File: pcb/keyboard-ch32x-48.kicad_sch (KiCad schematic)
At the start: 116 parts, among them J1 USB_C_Receptacle_USB2.0, J2 Conn_01x02, J3 Conn_01x04, SW1 SW_SPST, SW2 SW_SPST, U1 CH32X033F8P6

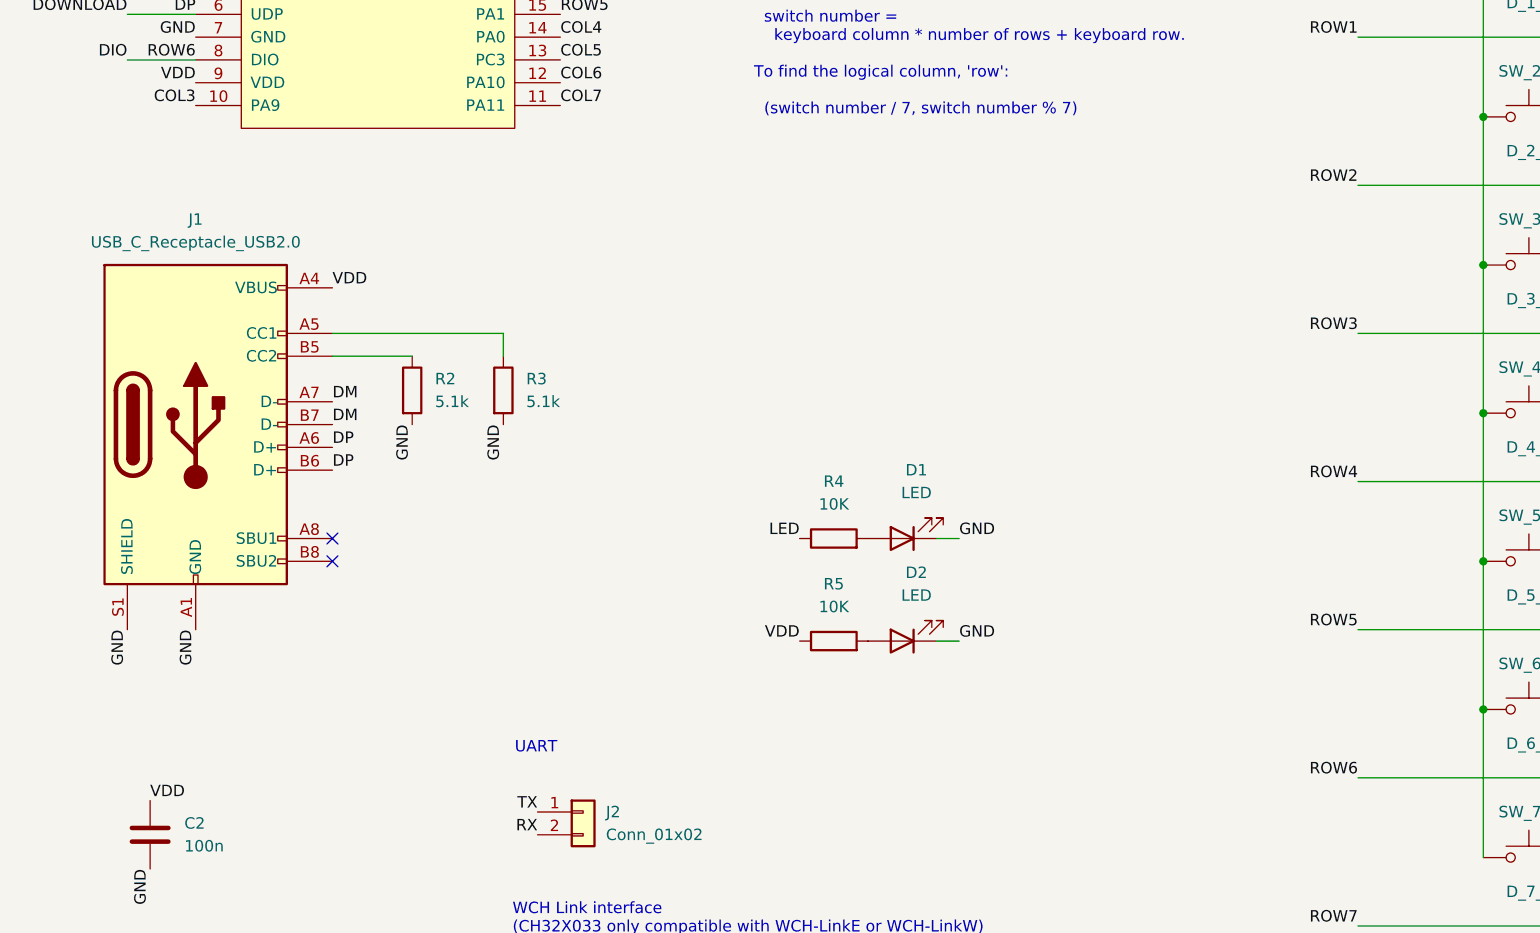
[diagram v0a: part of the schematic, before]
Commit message: pcb: ch32x-48: add notes to schematic
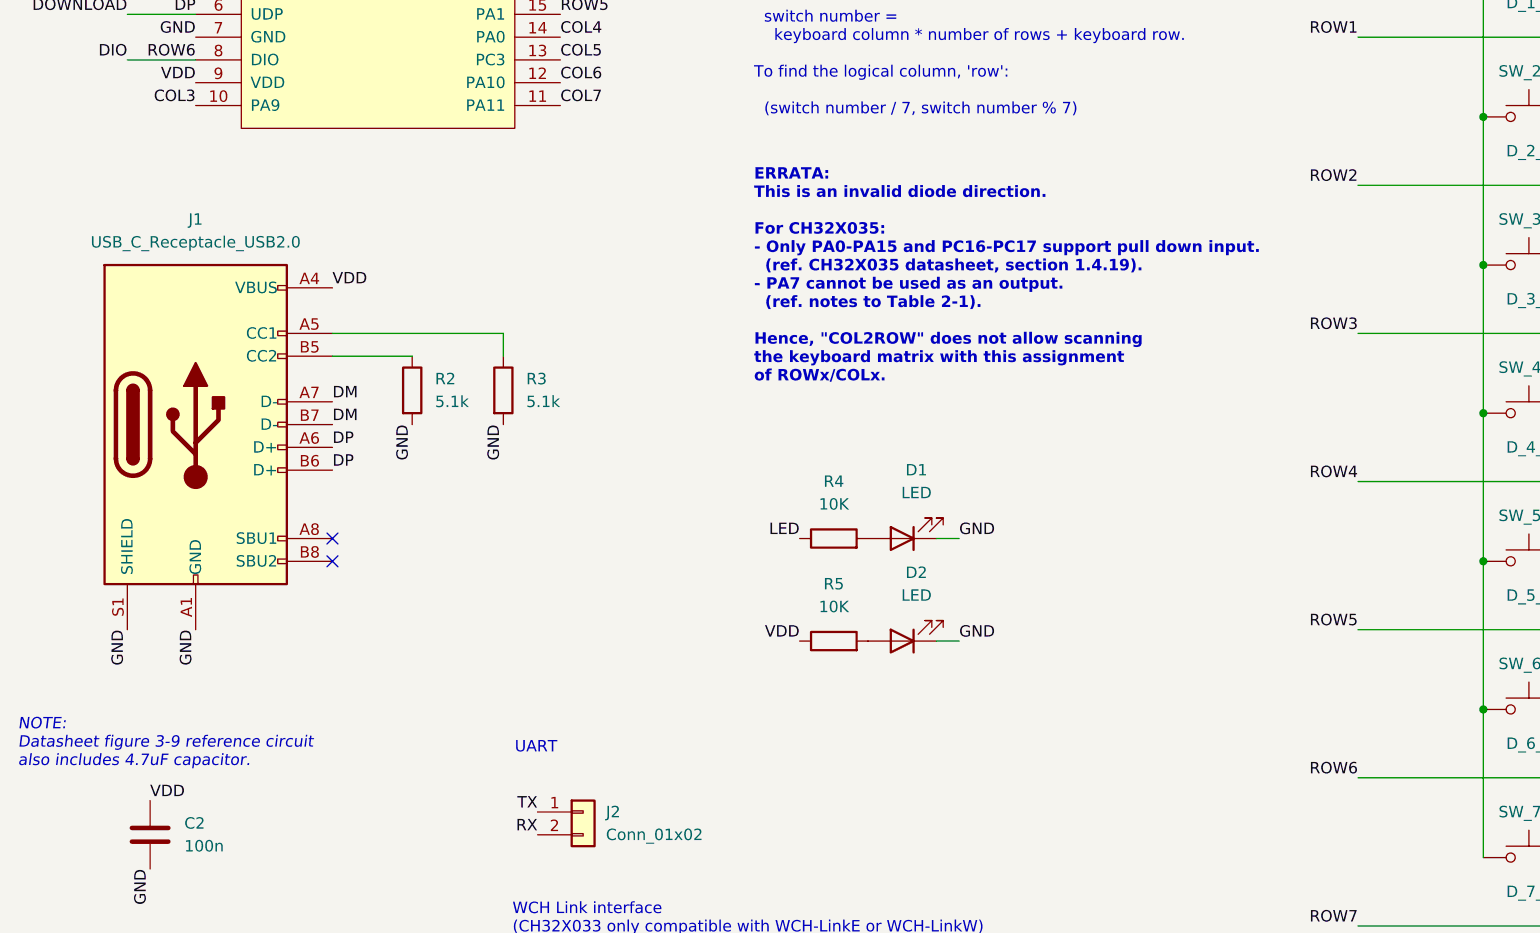
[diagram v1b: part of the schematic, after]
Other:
- note added: "ERRATA: This is an invalid diode direction. For CH32X035: - Only PA0-PA15 and PC16-PC17 support pull down input. (ref. CH32X035 datasheet, section 1.4.19). - PA7 cannot be used as an output. (ref. notes to Table 2-1). Hence, "COL2ROW" does not allow scanning the keyboard matrix with this assignment of ROWx/COLx."
- note added: "NOTE: Datasheet figure 3-9 reference circuit also includes 4.7uF capacitor."
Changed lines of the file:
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@@
+		)
+	)
+	(text "ERRATA:\nThis is an invalid diode direction.\n\nFor CH32X035:\n- Only PA0-PA15 and PC16-PC17 support pull down input.\n  (ref. CH32X035 datasheet, section 1.4.19).\n- PA7 cannot be used as an output.\n  (ref. notes to Table 2-1).\n\nHence, \"COL2ROW\" does not allow scanning\nthe keyboard matrix with this assignment\nof ROWx/COLx."
+		(exclude_from_sim no)
+		(at 96.52 66.04 0)
+		(effects
+			(font
+				(size 1.27 1.27)
+				(thickness 0.254)
+				(bold yes)
+				(color 255 0 0 1)
+			)
+			(justify left)
 		)
 	)
@@
 		)
 	)
+	(text "NOTE:\nDatasheet figure 3-9 reference circuit\nalso includes 4.7uF capacitor."
+		(exclude_from_sim no)
+		(at 14.478 118.11 0)
+		(effects
+			(font
+				(size 1.27 1.27)
+				(italic yes)
+				(color 0 194 0 1)
+			)
+			(justify left)
+		)
+	)

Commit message: pcb: ch32x-48: rev2025.2
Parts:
- added C3: 4.7uF, Capacitor_SMD:C_0805_2012Metric, symbol Device:C
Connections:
- net DCK: now also D_2_1.2 (A), D_2_2.2 (A), D_2_3.2 (A), D_2_4.2 (A), D_2_5.2 (A), D_2_6.2 (A), D_2_7.2 (A); no longer D_2_1.1 (K), D_2_2.1 (K), D_2_3.1 (K), D_2_4.1 (K), D_2_5.1 (K), D_2_6.1 (K), D_2_7.1 (K)
- net DIO: now also D_6_1.2 (A), D_6_2.2 (A), D_6_3.2 (A), D_6_4.2 (A), D_6_5.2 (A), D_6_6.2 (A), D_6_7.2 (A); no longer D_6_1.1 (K), D_6_2.1 (K), D_6_3.1 (K), D_6_4.1 (K), D_6_5.1 (K), D_6_6.1 (K), D_6_7.1 (K)
- net GND: now also C3.2
- net ROW1: now also D_1_1.2 (A), D_1_2.2 (A), D_1_3.2 (A), D_1_4.2 (A), D_1_5.2 (A), D_1_6.2 (A), D_1_7.2 (A); no longer D_1_1.1 (K), D_1_2.1 (K), D_1_3.1 (K), D_1_4.1 (K), D_1_5.1 (K), D_1_6.1 (K), D_1_7.1 (K)
- net ROW3: now also D_3_1.2 (A), D_3_2.2 (A), D_3_3.2 (A), D_3_4.2 (A), D_3_5.2 (A), D_3_6.2 (A), D_3_7.2 (A); no longer D_3_1.1 (K), D_3_2.1 (K), D_3_3.1 (K), D_3_4.1 (K), D_3_5.1 (K), D_3_6.1 (K), D_3_7.1 (K)
- net ROW4: now also D_4_1.2 (A), D_4_2.2 (A), D_4_3.2 (A), D_4_4.2 (A), D_4_5.2 (A), D_4_6.2 (A), D_4_7.2 (A); no longer D_4_1.1 (K), D_4_2.1 (K), D_4_3.1 (K), D_4_4.1 (K), D_4_5.1 (K), D_4_6.1 (K), D_4_7.1 (K)
- net ROW5: now also D_5_1.2 (A), D_5_2.2 (A), D_5_3.2 (A), D_5_4.2 (A), D_5_5.2 (A), D_5_6.2 (A), D_5_7.2 (A); no longer D_5_1.1 (K), D_5_2.1 (K), D_5_3.1 (K), D_5_4.1 (K), D_5_5.1 (K), D_5_6.1 (K), D_5_7.1 (K)
- net ROW7: now also D_7_1.2 (A), D_7_2.2 (A), D_7_3.2 (A), D_7_4.2 (A), D_7_5.2 (A), D_7_6.2 (A); no longer D_7_1.1 (K), D_7_2.1 (K), D_7_3.1 (K), D_7_4.1 (K), D_7_5.1 (K), D_7_6.1 (K)
- net VDD: now also C3.1
- net at SW_4_1.2: now also D_4_1.1 (K); no longer D_4_1.2 (A)
- net at SW_6_6.2: now also D_6_6.1 (K); no longer D_6_6.2 (A)
- net at SW_3_2.2: now also D_3_2.1 (K); no longer D_3_2.2 (A)
- net at SW_6_2.2: now also D_6_2.1 (K); no longer D_6_2.2 (A)
- net at SW_7_4.2: now also D_7_4.1 (K); no longer D_7_4.2 (A)
- net at SW_6_3.2: now also D_6_3.1 (K); no longer D_6_3.2 (A)
- net at SW_4_5.2: now also D_4_5.1 (K); no longer D_4_5.2 (A)
- net at SW_1_5.2: now also D_1_5.1 (K); no longer D_1_5.2 (A)
- net at SW_4_3.2: now also D_4_3.1 (K); no longer D_4_3.2 (A)
- net at SW_4_4.2: now also D_4_4.1 (K); no longer D_4_4.2 (A)
- net at SW_1_2.2: now also D_1_2.1 (K); no longer D_1_2.2 (A)
- net at SW_1_4.2: now also D_1_4.1 (K); no longer D_1_4.2 (A)
- net at SW_7_1.2: now also D_7_1.1 (K); no longer D_7_1.2 (A)
- net at SW_3_6.2: now also D_3_6.1 (K); no longer D_3_6.2 (A)
- net at SW_7_5.2: now also D_7_5.1 (K); no longer D_7_5.2 (A)
- net at SW_7_3.2: now also D_7_3.1 (K); no longer D_7_3.2 (A)
- net at SW_1_6.2: now also D_1_6.1 (K); no longer D_1_6.2 (A)
- net at SW_7_6.2: now also D_7_6.1 (K); no longer D_7_6.2 (A)
- net at SW_5_4.2: now also D_5_4.1 (K); no longer D_5_4.2 (A)
- net at SW_6_7.2: now also D_6_7.1 (K); no longer D_6_7.2 (A)
- net at SW_3_5.2: now also D_3_5.1 (K); no longer D_3_5.2 (A)
- net at SW_5_1.2: now also D_5_1.1 (K); no longer D_5_1.2 (A)
- net at SW_3_7.2: now also D_3_7.1 (K); no longer D_3_7.2 (A)
- net at SW_2_1.2: now also D_2_1.1 (K); no longer D_2_1.2 (A)
- net at SW_6_5.2: now also D_6_5.1 (K); no longer D_6_5.2 (A)
- net at SW_5_2.2: now also D_5_2.1 (K); no longer D_5_2.2 (A)
- net at SW_2_2.2: now also D_2_2.1 (K); no longer D_2_2.2 (A)
- net at SW_1_3.2: now also D_1_3.1 (K); no longer D_1_3.2 (A)
- net at SW_4_7.2: now also D_4_7.1 (K); no longer D_4_7.2 (A)
- net at SW_4_2.2: now also D_4_2.1 (K); no longer D_4_2.2 (A)
- net at SW_2_3.2: now also D_2_3.1 (K); no longer D_2_3.2 (A)
- net at SW_7_2.2: now also D_7_2.1 (K); no longer D_7_2.2 (A)
- net at SW_2_4.2: now also D_2_4.1 (K); no longer D_2_4.2 (A)
- net at SW_4_6.2: now also D_4_6.1 (K); no longer D_4_6.2 (A)
- net at SW_5_3.2: now also D_5_3.1 (K); no longer D_5_3.2 (A)
- net at SW_5_5.2: now also D_5_5.1 (K); no longer D_5_5.2 (A)
- net at SW_5_7.2: now also D_5_7.1 (K); no longer D_5_7.2 (A)
- net at SW_2_5.2: now also D_2_5.1 (K); no longer D_2_5.2 (A)
- net at SW_2_6.2: now also D_2_6.1 (K); no longer D_2_6.2 (A)
- net at SW_2_7.2: now also D_2_7.1 (K); no longer D_2_7.2 (A)
- net at SW_3_3.2: now also D_3_3.1 (K); no longer D_3_3.2 (A)
- net at SW_6_4.2: now also D_6_4.1 (K); no longer D_6_4.2 (A)
- net at SW_1_7.2: now also D_1_7.1 (K); no longer D_1_7.2 (A)
- net at SW_5_6.2: now also D_5_6.1 (K); no longer D_5_6.2 (A)
- net at SW_6_1.2: now also D_6_1.1 (K); no longer D_6_1.2 (A)
- net at SW_3_1.2: now also D_3_1.1 (K); no longer D_3_1.2 (A)
- net at SW_3_4.2: now also D_3_4.1 (K); no longer D_3_4.2 (A)
- net at SW_1_1.2: now also D_1_1.1 (K); no longer D_1_1.2 (A)
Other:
- note added: "Decoupling capacitors"
- note added: "Download switch. Short while plugging in USB to enter ISP flashing mode. e.g. with wchisp."
- note added: "Hardware, Mounting Holes For M2 screws. Same mounting holes as JJ40."
- note added: "IMPORTANT: Take care with diode direction!"
- note added: "Reset Switch ref. Figure 3-3 Typical circuit of CH32X datasheet."
- note added: "Take care the diode direction agrees with matrix scanning requirements for writing to the pin / pulling down."
- note added: "UART For simple printf debugging with UART2. ("ROW4"/SW_4_x switches can't be used while using UART2)."
- note added: "USB Connector"
- note added: "WCH Link interface (CH32X033 only compatible with WCH-LinkE or WCH-LinkW) Using DIO/DCK prevents use of ROW2/ROW6."
- note removed: "ERRATA: This is an invalid diode direction. For CH32X035: - Only PA0-PA15 and PC16-PC17 support pull down input. (ref. CH32X035 datasheet, section 1.4.19). - PA7 cannot be used as an output. (ref. notes to Table 2-1). Hence, "COL2ROW" does not allow scanning the keyboard matrix with this assignment of ROWx/COLx."
- note removed: "NOTE: Datasheet figure 3-9 reference circuit also includes 4.7uF capacitor."
- note removed: "UART"
- note removed: "WCH Link interface (CH32X033 only compatible with WCH-LinkE or WCH-LinkW)"
- moved on the sheet: C1, C2, D1, D2, D_1_1, D_1_2, D_1_3, D_1_4, D_1_5, D_1_6, D_1_7, D_2_1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

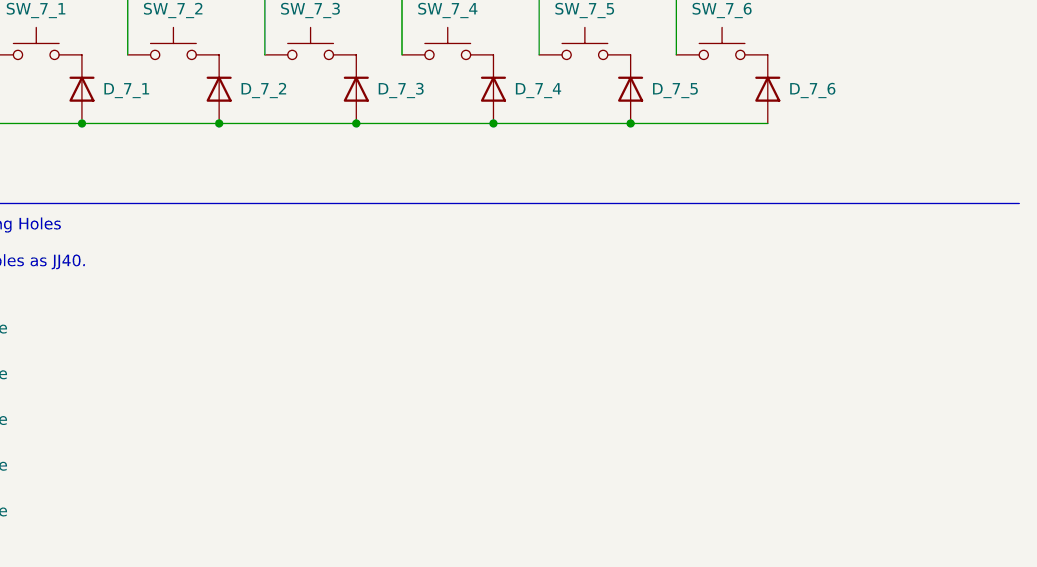
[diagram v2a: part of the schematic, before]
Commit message: pcb: ch32x-48 rev2025.3
rev2025.3:
- increase trace width to 0.25,
  - fix DRC.
- add 10K pullup for Row6 (DIO),
   per testing of the rev2025.1 board.

rev2025.2:
- fixed the diodes to be col2row,
  as the assignments of rows
  (and CH32X limitations on pins)
  required this.
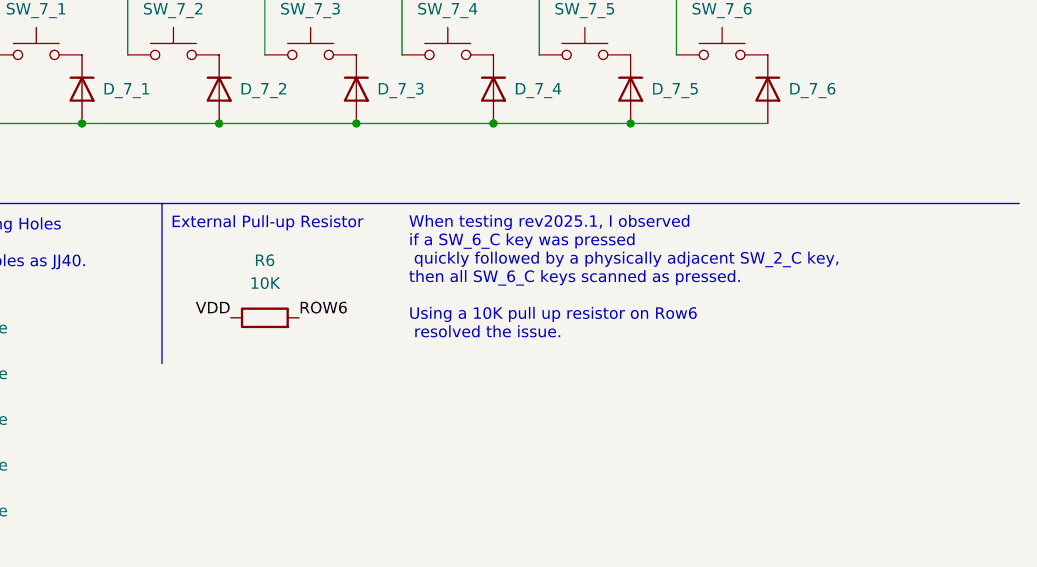
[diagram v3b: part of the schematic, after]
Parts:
- added R6: 10K, Resistor_SMD:R_0805_2012Metric, symbol Device:R
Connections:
- net DIO: now also R6.2
- net VDD: now also R6.1
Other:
- note added: "External Pull-up Resistor"
- note added: "When testing rev2025.1, I observed if a SW_6_C key was pressed quickly followed by a physically adjacent SW_2_C key, then all SW_6_C keys scanned as pressed. Using a 10K pull up resistor on Row6 resolved the issue."
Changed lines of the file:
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@@
 	(title_block
 		(title "CH32X-48")
-		(date "2025-01-10")
-		(rev "rev2025.2")
+		(date "2025-01-16")
+		(rev "rev2025.3")
 		(company "Richard Goulter (rgoulter)")
 		(comment 1 "48-key on 7x7 digital matrix.")
@@
 		)
 	)
+	(polyline
+		(pts
+			(xy 189.23 147.32) (xy 189.23 165.1)
+		)
+		(stroke
+			(width 0)
+			(type default)
+		)
+	)
 	(wire
 		(pts
@@
 		)
 	)
+	(text "External Pull-up Resistor"
+		(exclude_from_sim no)
+		(at 190.246 149.606 0)
+		(effects
+			(font
+				(size 1.27 1.27)
+			)
+			(justify left)
+		)
+	)
 	(text "Reset Switch\nref. Figure 3-3 Typical circuit\nof CH32X datasheet."
 		(exclude_from_sim no)
@@
 		)
 	)
+	(text "When testing rev2025.1, I observed\nif a SW_6_C key was pressed\n quickly followed by a physically adjacent SW_2_C key,\nthen all SW_6_C keys scanned as pressed.\n\nUsing a 10K pull up resistor on Row6\n resolved the issue."
+		(exclude_from_sim no)
+		(at 216.662 155.702 0)
+		(effects
+			(font
+				(size 1.27 1.27)
+			)
+			(justify left)
+		)
+	)
 	(text "Hardware, Mounting Holes\nFor M2 screws.\nSame mounting holes as JJ40."
 		(exclude_from_sim no)
@@
 		)
 	)
+	(label "ROW6"
+		(at 204.47 160.02 0)
+		(fields_autoplaced yes)
+		(effects
+			(font
+				(size 1.27 1.27)
+			)
+			(justify left bottom)
+		)
+	)
 	(label "COL2"
 		(at 34.29 24.13 180)
@@
 		)
 	)
+	(label "VDD"
+		(at 196.85 160.02 180)
+		(fields_autoplaced yes)
+		(effects
+			(font
+				(size 1.27 1.27)
+			)
+			(justify right bottom)
+		)
+	)
 	(label "COL6"
 		(at 246.38 21.59 90)
@@
 					(unit 1)
 				)
+			)
+		)
+	)
+	(symbol
+		(lib_id "Device:R")
+		(at 200.66 160.02 90)
+		(unit 1)
+		(exclude_from_sim no)
+		(in_bom yes)
+		(on_board yes)
+		(dnp no)
+		(fields_autoplaced yes)
+		(property "Reference" "R6"
+			(at 200.66 153.67 90)
+			(effects
+				(font
+					(size 1.27 1.27)
+				)
+			)
+		)
+		(property "Value" "10K"
+			(at 200.66 156.21 90)
+			(effects
+				(font
+					(size 1.27 1.27)
+				)
+			)
+		)
+		(property "Footprint" "Resistor_SMD:R_0805_2012Metric"
+			(at 200.66 161.798 90)
+			(effects
+				(font
+					(size 1.27 1.27)
+				)
+				(hide yes)
+			)
+		)
+		(property "Datasheet" "~"
+			(at 200.66 160.02 0)
+			(effects
+				(font
+					(size 1.27 1.27)
+				)
+				(hide yes)
+			)
+		)
+		(property "Description" ""
+			(at 200.66 160.02 0)
+			(effects
+				(font
+					(size 1.27 1.27)
+				)
+				(hide yes)
+			)
+		)
+		(property "LCSC" "C17414"
+			(at 200.66 160.02 0)
+			(effects
+				(font
+					(size 1.27 1.27)
+				)
+				(hide yes)
+			)
+		)
+		(pin "1"
+		)
+		(pin "2"
+		)
+		(instances
+			(project "keyboard-ch32x-48"
+				(path "/491af640-c615-48ab-84d8-9b166bc1ab37"
+					(reference "R6")
+					(unit 1)
+				)

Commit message: pcb: ch32x-48 rev2025.4
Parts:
- removed R6: 10K, Resistor_SMD:R_0805_2012Metric, symbol Device:R
- SW_1_1, SW_1_2, SW_1_3, SW_1_4, SW_1_5, SW_1_6, SW_1_7, SW_2_1, SW_2_2, SW_2_3, SW_2_4, SW_2_5, SW_2_6, SW_2_7, SW_3_1, SW_3_2, SW_3_3, SW_3_4, SW_3_5, SW_3_6, SW_3_7, SW_4_1, SW_4_2, SW_4_3, SW_4_4, SW_4_5, SW_4_6, SW_4_7, SW_5_1, SW_5_2, SW_5_3, SW_5_4, SW_5_5, SW_5_6, SW_5_7, SW_6_1, SW_6_2, SW_6_3, SW_6_4, SW_6_5, SW_6_6, SW_6_7, SW_7_1, SW_7_2, SW_7_3, SW_7_4, SW_7_5, SW_7_6: value MX-compatible or Kailh Choc v1 -> MX-compatible
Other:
- note added: "- Constraints on pin output: Since PA7 is used as ROWx, matrix scanning MUST use rows as inputs. - Constraints on pull-down input: Since PC18,PC19 are used as ROWx, matrix scanning MUST pull up rows. Hence, the diodes in the matrix must be "row to col"."
- note added: "LEDs"
- note added: "Microcontroller"
- note added: "NOTE: SWD (SDI) is enabled by default. This causes issues with matrix scanning on Row6. Refer to Reference Manual section on AFIO remap register for disabling SWD."
- note added: "Switch Matrix The keyboard has 48 keys laid out in a 4-row-12-column grid. It uses fewer GPIO pins to have a 7x7 matrix (14 pins) than to use a 4x12 (16 pins) matrix. The mapping is top-to-bottom, left-to-right. This retains "column X <= Y". To find the key number: switch number = keyboard column * number of rows + keyboard row. To find the logical column, 'row': (switch number / 7, switch number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"
- note added: "WCH Link interface (CH32X033 only compatible with WCH-LinkE or WCH-LinkW) Using DIO/DCK prevents use of ROW2/ROW6. SWD (SDI) enabled by default; must be disabled after reset."
- note removed: "External Pull-up Resistor"
- note removed: "Per the CH32X035 datasheet, PA7 can not be output."
- note removed: "The keyboard has 48 keys laid out in a 4-row-12-column grid. It uses fewer GPIO pins to have a 7x7 matrix (14 pins) than to use a 4x12 (16 pins) matrix. The mapping is top-to-bottom, left-to-right. This retains "column X <= Y". To find the key number: switch number = keyboard column * number of rows + keyboard row. To find the logical column, 'row': (switch number / 7, switch number % 7)"
- note removed: "WCH Link interface (CH32X033 only compatible with WCH-LinkE or WCH-LinkW) Using DIO/DCK prevents use of ROW2/ROW6."
- note removed: "When testing rev2025.1, I observed if a SW_6_C key was pressed quickly followed by a physically adjacent SW_2_C key, then all SW_6_C keys scanned as pressed. Using a 10K pull up resistor on Row6 resolved the issue."
- moved on the sheet: C1, C2, C3, D1, D2, J1, J2, J3, R1, R2, R3, R4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
